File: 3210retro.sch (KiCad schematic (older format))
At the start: 8 parts, among them P101 USB_OTG, P102 BAT, P103 DC, P105 EAR, P107 HEADPHONE, P109 RUMBLE, X101 ANT_GPS, X102 ANT_GSM

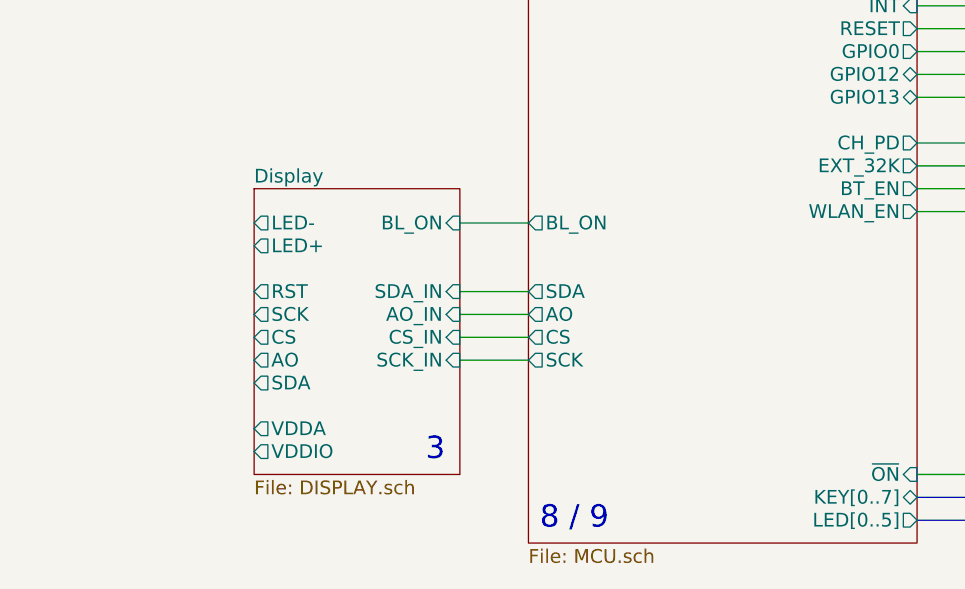
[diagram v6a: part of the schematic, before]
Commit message: Added Interface for OLED display
Added Booster for 4V -> 15V
Added bus for display data
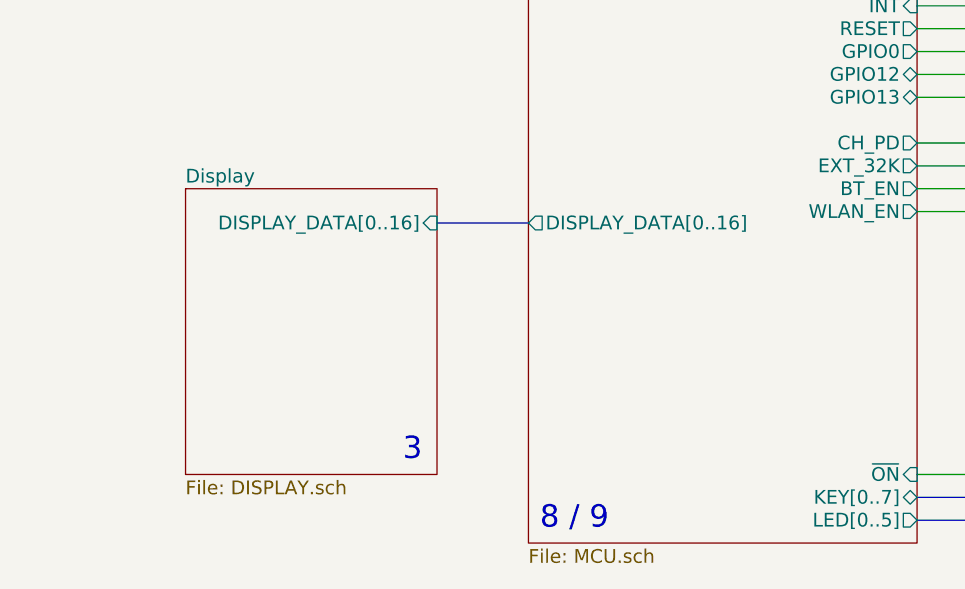
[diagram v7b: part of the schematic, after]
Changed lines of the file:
@@
 LIBS:lm4930
 LIBS:ts5a22366
+LIBS:tps61041dbv
 LIBS:3210retro-cache
 EELAYER 25 0
@@
 $EndSheet
 $Sheet
-S 2450 6050 900  1250
+S 2150 6050 1100 1250
 U 5805F4C1
 F0 "Display" 60
 F1 "DISPLAY.sch" 60
-F2 "VDDIO" O L 2450 7200 60
-F3 "VDDA" O L 2450 7100 60
-F4 "SDA" O L 2450 6900 60
-F5 "AO" O L 2450 6800 60
-F6 "CS" O L 2450 6700 60
-F7 "SCK" O L 2450 6600 60
-F8 "RST" O L 2450 6500 60
-F9 "LED+" O L 2450 6300 60
-F10 "LED-" O L 2450 6200 60
-F11 "SDA_IN" I R 3350 6500 60
-F12 "AO_IN" I R 3350 6600 60
-F13 "CS_IN" I R 3350 6700 60
-F14 "SCK_IN" I R 3350 6800 60
-F15 "BL_ON" I R 3350 6200 60
+F4 "DISPLAY_DATA[0..16]" I R 3250 6200 60
 $EndSheet
 $Comp
@@
 Wire Wire Line
 	10100 4000 10300 4000
-Wire Wire Line
-	3650 6500 3350 6500
-Wire Wire Line
-	3350 6600 3650 6600
-Wire Wire Line
-	3650 6700 3350 6700
-Wire Wire Line
-	3350 6800 3650 6800
-Wire Wire Line
-	3650 6200 3350 6200
 $Sheet
 S 5600 7200 1150 400
@@
 F7 "RADIO_ON" O R 5350 2000 60
 F8 "RADIO_ACTIVE" O R 5350 2100 60
-F9 "SDA" O L 3650 6500 60
-F10 "AO" O L 3650 6600 60
-F11 "CS" O L 3650 6700 60
-F12 "SCK" O L 3650 6800 60
-F13 "BL_ON" O L 3650 6200 60
-F14 "D+" B L 3650 3000 60
-F15 "D-" B L 3650 2900 60
-F16 "USB_OTG_ID" O L 3650 3100 60
-F17 "VBAT_ref" I L 3650 2200 60
-F18 "V_USB_BUS_ref" I L 3650 2300 60
-F19 "VDC_ref" I L 3650 2400 60
-F20 "~CHARGING" I L 3650 2700 60
-F21 "3V3_PG" I L 3650 2500 60
-F22 "GPS_TX" I R 5350 2700 60
-F23 "~LINK_UP" I R 5350 5150 60
-F24 "~INT" I R 5350 5250 60
-F25 "RESET" O R 5350 5350 60
-F26 "GPIO0" O R 5350 5450 60
-F27 "KEY[0..7]" B R 5350 7400 60
-F28 "LED[0..5]" O R 5350 7500 60
-F29 "ESP_UART[0..3]" B R 5350 4400 60
-F30 "BT[0..7]" B R 5350 4600 60
-F31 "WL[0..6]" B R 5350 4800 60
-F32 "UART[0..3]" B R 5350 2300 60
-F33 "HST_DL[0..1]" B R 5350 2500 60
-F34 "CH_PD" O R 5350 5850 60
-F35 "EXT_32K" O R 5350 5950 60
-F36 "BT_EN" O R 5350 6050 60
-F37 "WLAN_EN" O R 5350 6150 60
-F38 "GPIO12" B R 5350 5550 60
-F39 "GPIO13" B R 5350 5650 60
+F9 "D+" B L 3650 3000 60
+F10 "D-" B L 3650 2900 60
+F11 "USB_OTG_ID" O L 3650 3100 60
+F12 "VBAT_ref" I L 3650 2200 60
+F13 "V_USB_BUS_ref" I L 3650 2300 60
+F14 "VDC_ref" I L 3650 2400 60
+F15 "~CHARGING" I L 3650 2700 60
+F16 "3V3_PG" I L 3650 2500 60
+F17 "GPS_TX" I R 5350 2700 60
+F18 "~LINK_UP" I R 5350 5150 60
+F19 "~INT" I R 5350 5250 60
+F20 "RESET" O R 5350 5350 60
+F21 "GPIO0" O R 5350 5450 60
+F22 "KEY[0..7]" B R 5350 7400 60
+F23 "LED[0..5]" O R 5350 7500 60
+F24 "ESP_UART[0..3]" B R 5350 4400 60
+F25 "BT[0..7]" B R 5350 4600 60
+F26 "WL[0..6]" B R 5350 4800 60
+F27 "UART[0..3]" B R 5350 2300 60
+F28 "HST_DL[0..1]" B R 5350 2500 60
+F29 "CH_PD" O R 5350 5850 60
+F30 "EXT_32K" O R 5350 5950 60
+F31 "BT_EN" O R 5350 6050 60
+F32 "WLAN_EN" O R 5350 6150 60
+F33 "GPIO12" B R 5350 5550 60
+F34 "GPIO13" B R 5350 5650 60
+F35 "DISPLAY_DATA[0..16]" O L 3650 6200 60
 $EndSheet
 Wire Wire Line
@@
 Text Notes 3700 7550 0    98   ~ 0
 8 / 9
-Text Notes 3200 7250 0    98   ~ 0
+Text Notes 3100 7250 0    98   ~ 0
 3
 Text Notes 9100 4200 0    98   ~ 0
@@
 Text Notes 1600 2900 0    59   ~ 0
 50Ohm
+Wire Bus Line
+	3650 6200 3250 6200
 $EndSCHEMATC

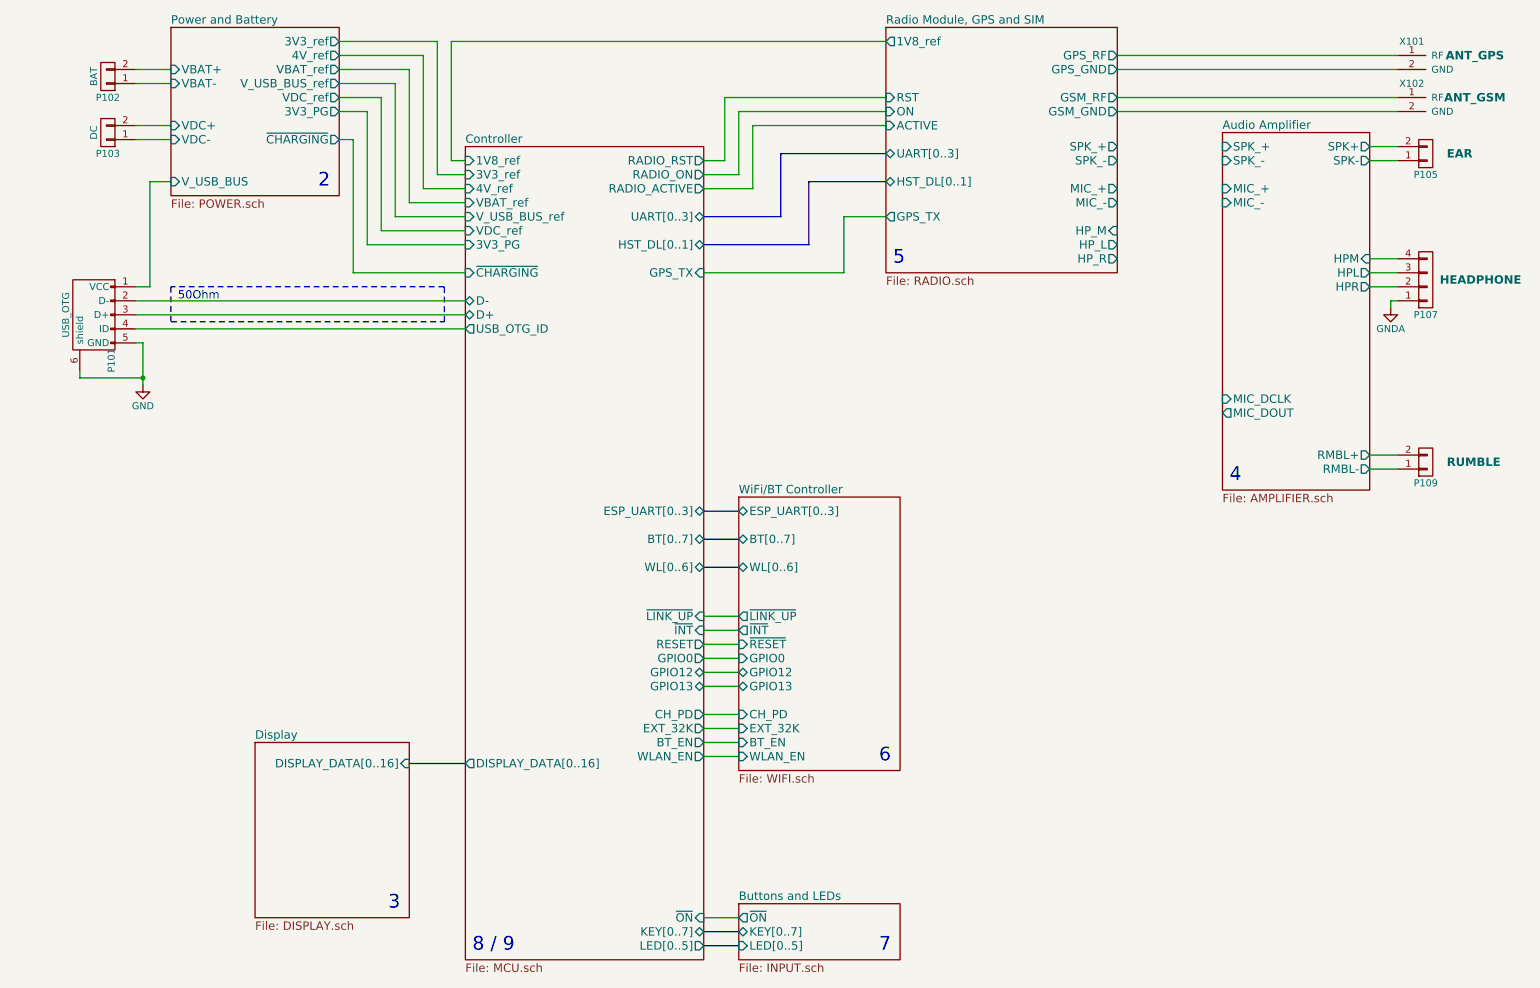
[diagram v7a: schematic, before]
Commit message: Removed WiFi Module added Footprints
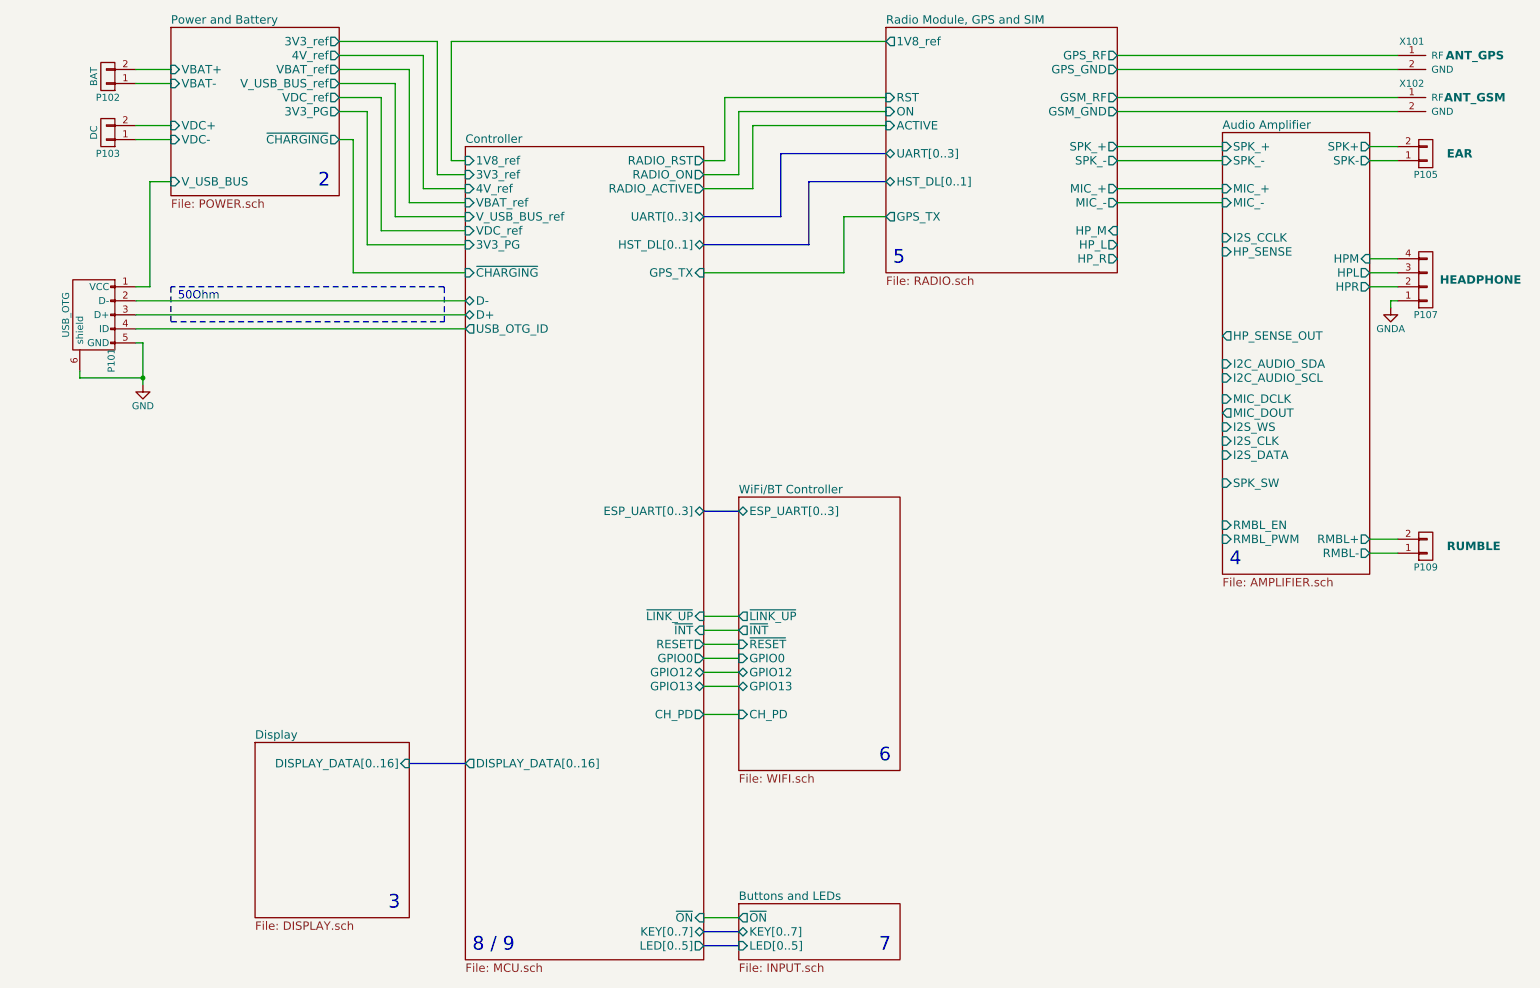
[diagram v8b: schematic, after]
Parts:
- P101: footprint (none) -> Connectors_Molex:USB_Micro-B_Molex_47346-0001
- X101, X102: footprint (none) -> SMD_Packages:1Pin
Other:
- moved on the sheet: P109
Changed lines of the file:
@@
 F0 "Display" 60
 F1 "DISPLAY.sch" 60
-F4 "DISPLAY_DATA[0..16]" I R 3250 6200 60
+F2 "DISPLAY_DATA[0..16]" I R 3250 6200 60
 $EndSheet
 $Comp
@@
 	1300 1250 1550 1250
 $Sheet
-S 9050 1700 1050 2550
+S 9050 1700 1050 3150
 U 5805F4B1
 F0 "Audio Amplifier" 60
@@
 F9 "HPL" O R 10100 2700 60
 F10 "HPR" O R 10100 2800 60
-F11 "RMBL+" O R 10100 4000 60
+F11 "RMBL+" O R 10100 4600 60
 F12 "MIC_DCLK" I L 9050 3600 60
 F13 "MIC_DOUT" O L 9050 3700 60
-F14 "RMBL-" O R 10100 4100 60
+F14 "RMBL-" O R 10100 4700 60
+F15 "RMBL_PWM" I L 9050 4600 60
+F16 "RMBL_EN" I L 9050 4500 60
+F17 "I2S_DATA" I L 9050 4000 60
+F18 "I2S_CLK" I L 9050 3900 60
+F19 "I2S_WS" I L 9050 3800 60
+F20 "HP_SENSE" I L 9050 2550 60
+F21 "I2S_CCLK" I L 9050 2450 60
+F22 "HP_SENSE_OUT" O L 9050 3150 60
+F23 "SPK_SW" I L 9050 4200 60
+F24 "I2C_AUDIO_SDA" I L 9050 3350 60
+F25 "I2C_AUDIO_SCL" I L 9050 3450 60
 $EndSheet
 $Comp
@@
 F 0 "X102" H 10400 1550 50  0000 C CNN
 F 1 "ANT_GSM" H 10850 1450 60  0000 C CNB
-F 2 "" H 10300 1450 60  0001 C CNN
+F 2 "SMD_Packages:1Pin" H 10300 1450 60  0001 C CNN
 F 3 "" H 10300 1450 60  0000 C CNN
 	1    10300 1450
@@
 F 0 "X101" H 10400 1250 50  0000 C CNN
 F 1 "ANT_GPS" H 10850 1150 60  0000 C CNB
-F 2 "" H 10300 1150 60  0001 C CNN
+F 2 "SMD_Packages:1Pin" H 10300 1150 60  0001 C CNN
 F 3 "" H 10300 1150 60  0000 C CNN
 	1    10300 1150
@@
 F 0 "P101" H 1325 2875 50  0000 C CNN
 F 1 "USB_OTG" H 1000 3200 50  0000 C CNN
-F 2 "" V 950 2900 50  0001 C CNN
+F 2 "Connectors_Molex:USB_Micro-B_Molex_47346-0001" V 950 2900 50  0001 C CNN
 F 3 "" V 950 2900 50  0000 C CNN
 	1    1000 3000
@@
 $EndComp
 $Comp
-L GND #PWR03
+L GND #PWR02
 U 1 1 580BB0C9
 P 1350 3500
-F 0 "#PWR03" H 1350 3250 50  0001 C CNN
+F 0 "#PWR02" H 1350 3250 50  0001 C CNN
 F 1 "GND" H 1350 3350 50  0000 C CNN
 F 2 "" H 1350 3500 50  0000 C CNN
@@
 F4 "~RESET" I L 5600 5350 60
 F5 "GPIO0" I L 5600 5450 60
-F6 "EXT_32K" I L 5600 5950 60
-F7 "BT_EN" I L 5600 6050 60
 F8 "ESP_UART[0..3]" B L 5600 4400 60
-F9 "BT[0..7]" B L 5600 4600 60
-F10 "WLAN_EN" I L 5600 6150 60
-F11 "WL[0..6]" B L 5600 4800 60
 F12 "CH_PD" I L 5600 5850 60
 F13 "GPIO12" B L 5600 5550 60
@@
 L CONN_01X02 P109
 U 1 1 580EBF81
-P 10500 4050
-F 0 "P109" H 10500 4200 50  0000 C CNN
-F 1 "RUMBLE" H 10650 4050 60  0000 L CNB
-F 2 "Pin_Headers:Pin_Header_Straight_1x02" H 10500 4050 50  0001 C CNN
-F 3 "" H 10500 4050 50  0000 C CNN
-	1    10500 4050
+P 10500 4650
+F 0 "P109" H 10500 4800 50  0000 C CNN
+F 1 "RUMBLE" H 10650 4650 60  0000 L CNB
+F 2 "Pin_Headers:Pin_Header_Straight_1x02" H 10500 4650 50  0001 C CNN
+F 3 "" H 10500 4650 50  0000 C CNN
+	1    10500 4650
 	1    0    0    1
 $EndComp
@@
 	5600 5450 5350 5450
 Wire Wire Line
-	10100 4100 10300 4100
-Wire Wire Line
-	10100 4000 10300 4000
+	10100 4700 10300 4700
+Wire Wire Line
+	10100 4600 10300 4600
 $Sheet
 S 5600 7200 1150 400
@@
 F4 "LED[0..5]" I L 5600 7500 60
 $EndSheet
+Wire Wire Line
+	5350 7300 5600 7300
+Wire Bus Line
+	5350 7500 5600 7500
+Wire Bus Line
+	5350 7400 5600 7400
+Wire Bus Line
+	5350 4400 5600 4400
+Wire Bus Line
+	6650 1850 5900 1850
+Wire Bus Line
+	5900 1850 5900 2300
+Wire Bus Line
+	5900 2300 5350 2300
+Wire Bus Line
+	6650 2050 6100 2050
+Wire Bus Line
+	6100 2050 6100 2500
+Wire Bus Line
+	6100 2500 5350 2500
+Wire Wire Line
+	5350 5850 5600 5850
+Wire Wire Line
+	5350 5650 5600 5650
+Wire Wire Line
+	5600 5550 5350 5550
+Text Notes 2600 2100 0    98   ~ 0
+2
+Text Notes 6700 2650 0    98   ~ 0
+5
+Text Notes 6600 6200 0    98   ~ 0
+6
+Text Notes 3700 7550 0    98   ~ 0
+8 / 9
+Text Notes 3100 7250 0    98   ~ 0
+3
+Text Notes 9100 4800 0    98   ~ 0
+4
+Text Notes 6600 7550 0    98   ~ 0
+7
+Wire Notes Line
+	1550 2800 1550 3050
+Wire Notes Line
+	1550 3050 3500 3050
+Wire Notes Line
+	3500 3050 3500 2800
+Wire Notes Line
+	3500 2800 1550 2800
+Text Notes 1600 2900 0    59   ~ 0
+50Ohm
+Wire Bus Line
+	3650 6200 3250 6200
 $Sheet
 S 3650 1800 1700 5800
@@
 F23 "LED[0..5]" O R 5350 7500 60
 F24 "ESP_UART[0..3]" B R 5350 4400 60
-F25 "BT[0..7]" B R 5350 4600 60
-F26 "WL[0..6]" B R 5350 4800 60
 F27 "UART[0..3]" B R 5350 2300 60
 F28 "HST_DL[0..1]" B R 5350 2500 60
 F29 "CH_PD" O R 5350 5850 60
-F30 "EXT_32K" O R 5350 5950 60
-F31 "BT_EN" O R 5350 6050 60
-F32 "WLAN_EN" O R 5350 6150 60
 F33 "GPIO12" B R 5350 5550 60
 F34 "GPIO13" B R 5350 5650 60
@@
 $EndSheet
 Wire Wire Line
-	5350 7300 5600 7300
-Wire Bus Line
-	5350 7500 5600 7500
-Wire Bus Line
-	5350 7400 5600 7400
-Wire Bus Line
-	5350 4400 5600 4400
-Wire Bus Line
-	6650 1850 5900 1850
-Wire Bus Line
-	5900 1850 5900 2300
-Wire Bus Line
-	5900 2300 5350 2300
-Wire Bus Line
-	6650 2050 6100 2050
-Wire Bus Line
-	6100 2050 6100 2500
-Wire Bus Line
-	6100 2500 5350 2500
-Wire Bus Line
-	5600 4800 5350 4800
-Wire Bus Line
-	5350 4600 5600 4600
-Wire Wire Line
-	5350 5850 5600 5850
-Wire Wire Line
-	5600 5950 5350 5950
-Wire Wire Line
-	5350 6050 5600 6050
-Wire Wire Line
-	5600 6150 5350 6150
-Wire Wire Line
-	5350 5650 5600 5650
-Wire Wire Line
-	5600 5550 5350 5550
-Text Notes 2600 2100 0    98   ~ 0
-2
-Text Notes 6700 2650 0    98   ~ 0
-5
-Text Notes 6600 6200 0    98   ~ 0
-6
-Text Notes 3700 7550 0    98   ~ 0
-8 / 9
-Text Notes 3100 7250 0    98   ~ 0
-3
-Text Notes 9100 4200 0    98   ~ 0
-4
-Text Notes 6600 7550 0    98   ~ 0
-7
-Wire Notes Line
-	1550 2800 1550 3050
-Wire Notes Line
-	1550 3050 3500 3050
-Wire Notes Line
-	3500 3050 3500 2800
-Wire Notes Line
-	3500 2800 1550 2800
-Text Notes 1600 2900 0    59   ~ 0
-50Ohm
-Wire Bus Line
-	3650 6200 3250 6200
+	9050 1800 8300 1800
+Wire Wire Line
+	8300 1900 9050 1900
+Wire Wire Line
+	9050 2100 8300 2100
+Wire Wire Line
+	8300 2200 9050 2200
 $EndSCHEMATC
